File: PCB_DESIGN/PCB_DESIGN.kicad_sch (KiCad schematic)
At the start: 1 part, among them U1 A4988SETTR-T

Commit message: Actualizacion
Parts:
- removed U1: A4988SETTR-T, A4988_motorCtrl:QFN50P500X500X90-29N, symbol A4988SETTR-T:A4988SETTR-T
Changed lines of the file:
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@@
 	(generator_version "8.0")
 	(paper "A4")
-	(symbol
-		(lib_id "A4988SETTR-T:A4988SETTR-T")
-		(at 80.01 78.74 0)
-		(unit 1)
-		(exclude_from_sim no)
-		(in_bom yes)
-		(on_board yes)
-		(dnp no)
-		(fields_autoplaced yes)
-		(property "Reference" "U1"
-			(at 80.01 45.72 0)
-			(effects
-				(font
-					(size 1.27 1.27)
-				)
-			)
-		)
-		(property "Value" "A4988SETTR-T"
-			(at 80.01 48.26 0)
-			(effects
-				(font
-					(size 1.27 1.27)
-				)
-			)
-		)
-		(property "Footprint" "A4988_motorCtrl:QFN50P500X500X90-29N"
-			(at 80.01 78.74 0)
-			(effects
-				(font
-					(size 1.27 1.27)
-				)
-				(justify bottom)
-				(hide yes)
-			)
-		)
-		(property "Datasheet" ""
-			(at 80.01 78.74 0)
-			(effects
-				(font
-					(size 1.27 1.27)
-				)
-				(hide yes)
-			)
-		)
-		(property "Description" ""
-			(at 80.01 78.74 0)
-			(effects
-				(font
-					(size 1.27 1.27)
-				)
-				(hide yes)
-			)
-		)
-		(property "MANUFACTURER" "Allegro MicroSystems"
-			(at 80.01 78.74 0)
-			(effects
-				(font
-					(size 1.27 1.27)
-				)
-				(justify bottom)
-				(hide yes)
-			)
-		)
-		(pin "21"
-		)
-		(pin "8"
-		)
-		(pin "1"
-		)
-		(pin "24"
-		)
-		(pin "23"
-		)
-		(pin "5"
-		)
-		(pin "22"
-		)
-		(pin "29"
-		)
-		(pin "19"
-		)
-		(pin "18"
-		)
-		(pin "13"
-		)
-		(pin "27"
-		)
-		(pin "15"
-		)
-		(pin "10"
-		)
-		(pin "11"
-		)
-		(pin "9"
-		)
-		(pin "3"
-		)
-		(pin "12"
-		)
-		(pin "2"
-		)
-		(pin "26"
-		)
-		(pin "16"
-		)
-		(pin "4"
-		)
-		(pin "6"
-		)
-		(pin "28"
-		)
-		(pin "14"
-		)
-		(pin "17"
-		)
-		(instances
-			(project ""
-				(path "/e56d7197-46c3-4c96-a42c-d0ff3339c143"
-					(reference "U1")
-					(unit 1)
-				)
-			)
-		)
-	)
 	(sheet_instances
 		(path "/"

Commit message: Se actualiza el esquematico de la pcb
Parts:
- added C1, C10, C16, C7, C8: 0.1uF, Capacitor_SMD:C_0603_1608Metric_Pad1.08x0.95mm_HandSolder, symbol Device:C
- added C11, C5, C6, C9: C, Capacitor_SMD:C_0603_1608Metric_Pad1.08x0.95mm_HandSolder, symbol Device:C
- added C12, C14: 470μF, Capacitor_SMD:CP_Elec_4x5.3, symbol Device:C_Polarized
- added C13, C15: 0.1μF, Capacitor_SMD:C_0603_1608Metric_Pad1.08x0.95mm_HandSolder, symbol Device:C
- added C2: 0.47uF, Capacitor_SMD:C_0603_1608Metric_Pad1.08x0.95mm_HandSolder, symbol Device:C
- added C3: 10nF, Capacitor_SMD:C_0603_1608Metric_Pad1.08x0.95mm_HandSolder, symbol Device:C
- added C4: 100uF, Capacitor_SMD:CP_Elec_4x5.3, symbol Device:C_Polarized
- added D1: D_Schottky_Small, Diode_SMD:D_SMA, symbol Device:D_Schottky_Small
- added J1, J2: Screw_Terminal_01x04, Connector_PinHeader_2.54mm:PinHeader_1x04_P2.54mm_Vertical, symbol Connector:Screw_Terminal_01x04
- added L1: 47μH, Inductor_SMD:L_Cenker_CKCS5020, symbol Device:L
- added R1, R2: 0.10, Resistor_SMD:R_0603_1608Metric_Pad0.98x0.95mm_HandSolder, symbol Device:R
- added R3: 10k, Resistor_SMD:R_0603_1608Metric_Pad0.98x0.95mm_HandSolder, symbol Device:R
- added R4, R7, R8, R9: R, Resistor_SMD:R_0603_1608Metric_Pad0.98x0.95mm_HandSolder, symbol Device:R
- added RV1: 10k, Potentiometer_SMD:Potentiometer_Bourns_3314J_Vertical, symbol Device:R_Potentiometer
- added RV2: R_Potentiometer, Connector_PinHeader_2.54mm:PinHeader_1x03_P2.54mm_Vertical, symbol Device:R_Potentiometer
- added SW1, SW3: SW_Push, Connector_PinHeader_2.54mm:PinHeader_1x02_P2.54mm_Vertical, symbol Switch:SW_Push
- added U1: DRV8825PWP, DRV8825:IC_TPS61196PWPRQ1, symbol DRV8825PWP:DRV8825PWP
- added U2: ATmega328P-MM, Package_DFN_QFN:QFN-28-1EP_4x4mm_P0.45mm_EP2.4x2.4mm, symbol MCU_Microchip_ATmega:ATmega328P-MM
- added U3, U5: 74HC14, symbol 74xx:74HC14
- added U6: LM2596S-5, Package_TO_SOT_SMD:TO-263-5_TabPin3, symbol Regulator_Switching:LM2596S-5
- added Y1: 16 Mhz, Crystal:Crystal_SMD_0603-2Pin_6.0x3.5mm, symbol Device:Crystal
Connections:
- new net: R4.1, R7.1, SW1.1
- new net: C3.1, U1.2 (CP2)
- new net: C3.2, U1.1 (CP1)
- new net: RV1.2, U1.12 (AVREF), U1.13 (BVREF)
- new net: C1.1, U1.3 (VCP)
- new net: R1.1, U1.6 (ISENA)
- new net: R2.1, U1.9 (ISENB)
- new net: C9.2, R7.2, U3.1
- new net: R8.1, R9.1, SW3.1
- new net: C11.2, R9.2, U5.1
- new net: C5.1, U2.5 (XTAL1/PB6), Y1.2
- new net: R3.1, U2.25 (~{RESET}/PC6)
- new net: C6.1, U2.6 (XTAL2/PB7), Y1.1
- new net: D1.1 (K), L1.1, U6.2 (OUT)
- new net 24V: C1.2, C10.1, C12.1, C13.1, C16.1, C4.1, U1.11 (VMB), U1.4 (VMA), U6.1 (VIN)
- new net 3.3V: C2.1, RV1.1, U1.15 (V3P3OUT)
- new net 5V: C14.1, C15.1, C7.2, C8.1, J1.1 (Pin_1), L1.2, R3.2, SW1.2, SW3.2, U2.16 (AVCC), U2.3 (VCC), U6.4 (FB)
- new net A1: J2.4 (Pin_4), U1.5 (AOUT1)
- new net A2: J2.3 (Pin_3), U1.7 (AOUT2)
- new net B1: J2.2 (Pin_2), U1.10 (BOUT1)
- new net B2: J2.1 (Pin_1), U1.8 (BOUT2)
- new net DIR: U1.20 (DIR), U2.11 (PB1)
- new net GND: C10.2, C11.1, C12.2, C13.2, C14.2, C15.2, C16.2, C2.2, C4.2, C5.2, C6.2, C7.1, C8.2, C9.1, D1.2 (A), J1.4 (Pin_4), R1.2, R2.2, R4.2, R8.2, RV1.3, RV2.1, U1.14 (GND), U1.28 (GND__1), U1.29 (EXP), U1.30 (EXP__1), U1.31 (EXP__2), U1.32 (EXP__3), U1.33 (EXP__4), U1.34 (EXP__5), U1.35 (EXP__6), U1.36 (EXP__7), U1.37 (EXP__8), U1.38 (EXP__9), U1.39 (EXP__10), U1.40 (EXP__11), U1.41 (EXP__12), U1.42 (EXP__13), U1.43 (EXP__14), U1.44 (EXP__15), U1.45 (EXP__16), U1.46 (EXP__17), U1.47 (EXP__18), U1.48 (EXP__19), U1.49 (EXP__20), U1.50 (EXP__21), U2.18 (GND), U2.29 (GND), U2.4 (GND), U6.3 (GND), U6.5 (~{ON}/OFF)
- new net M1: U1.24 (MODE0)
- new net M2: U1.25 (MODE1), U2.12 (PB2)
- new net M3: U1.26 (MODE2)
- new net NRESET: U1.16 (~{NRESET})
- new net NSLEEP: U1.17 (NSLEEP), U2.14 (PB4)
- new net POT: RV2.2, U2.22 (PC3)
- new net PULSADOR1: U2.13 (PB3)
- new net PULSADOR2: U2.15 (PB5), U3.2, U5.2
- new net PULSADOR3: U2.27 (PD1)
- new net SCL: J1.2 (Pin_2), U2.24 (PC5)
- new net SDA: J1.3 (Pin_3), U2.23 (PC4)
- new net STEP: U1.22 (STEP), U2.1 (PD3)
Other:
- note added: "Lm2596 volt regulator (fixed output) 24Vcc - 5Vcc"

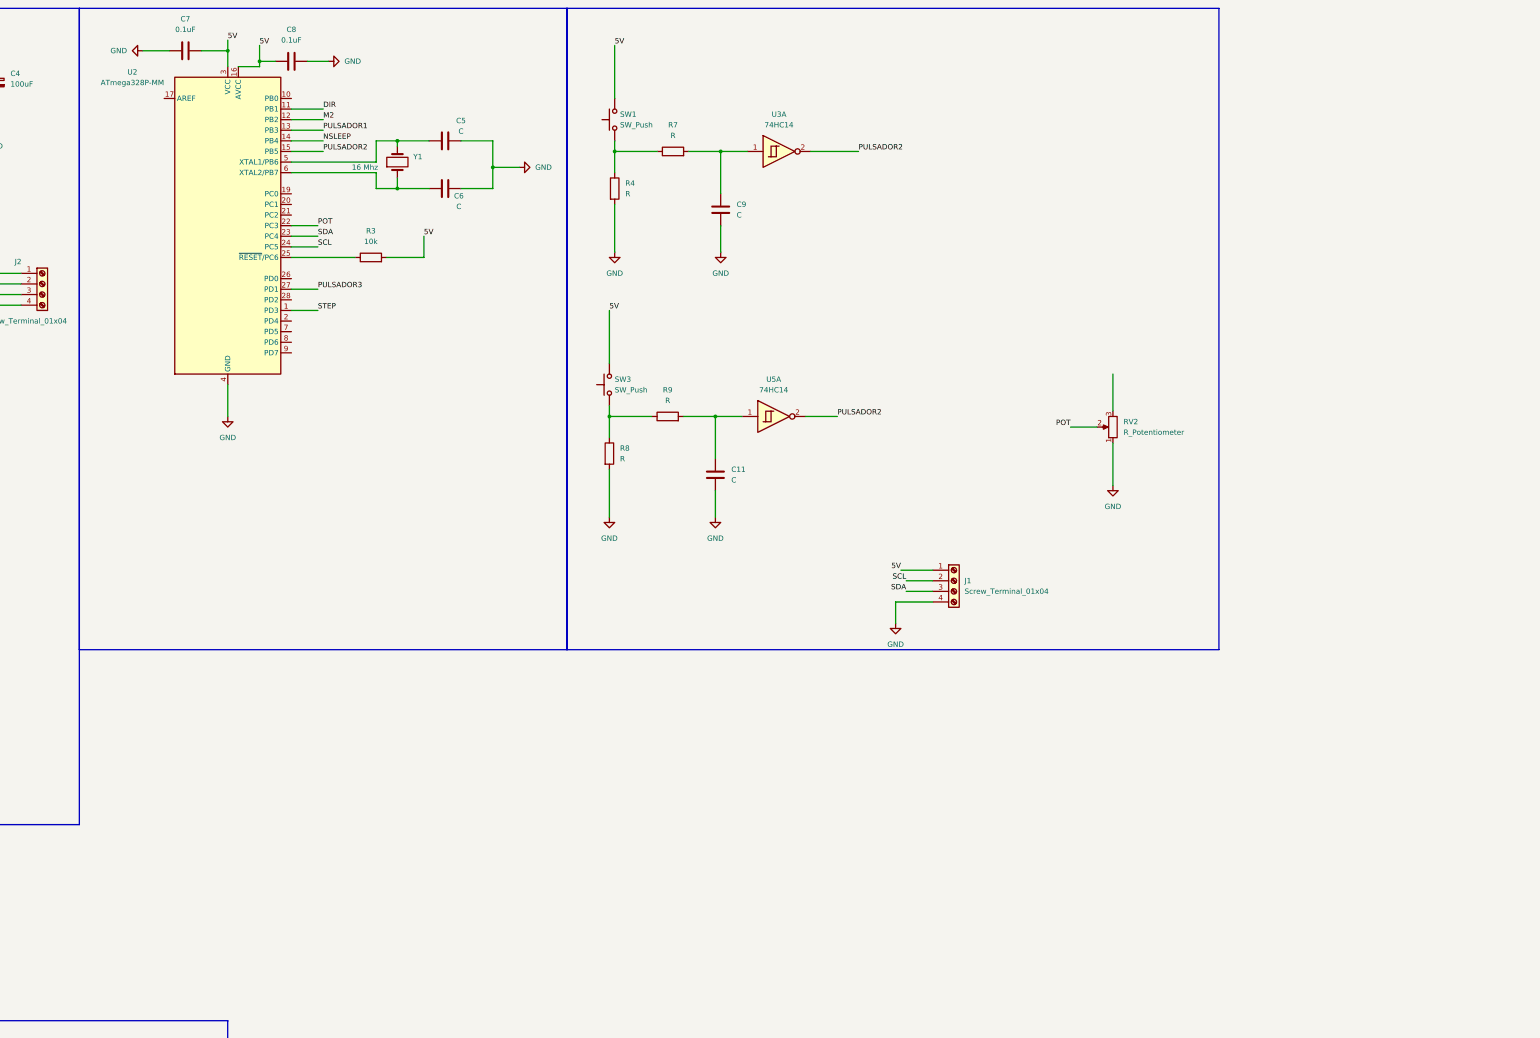
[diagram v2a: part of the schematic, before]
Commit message: Se actualiza el esquematico y se manda a pcb
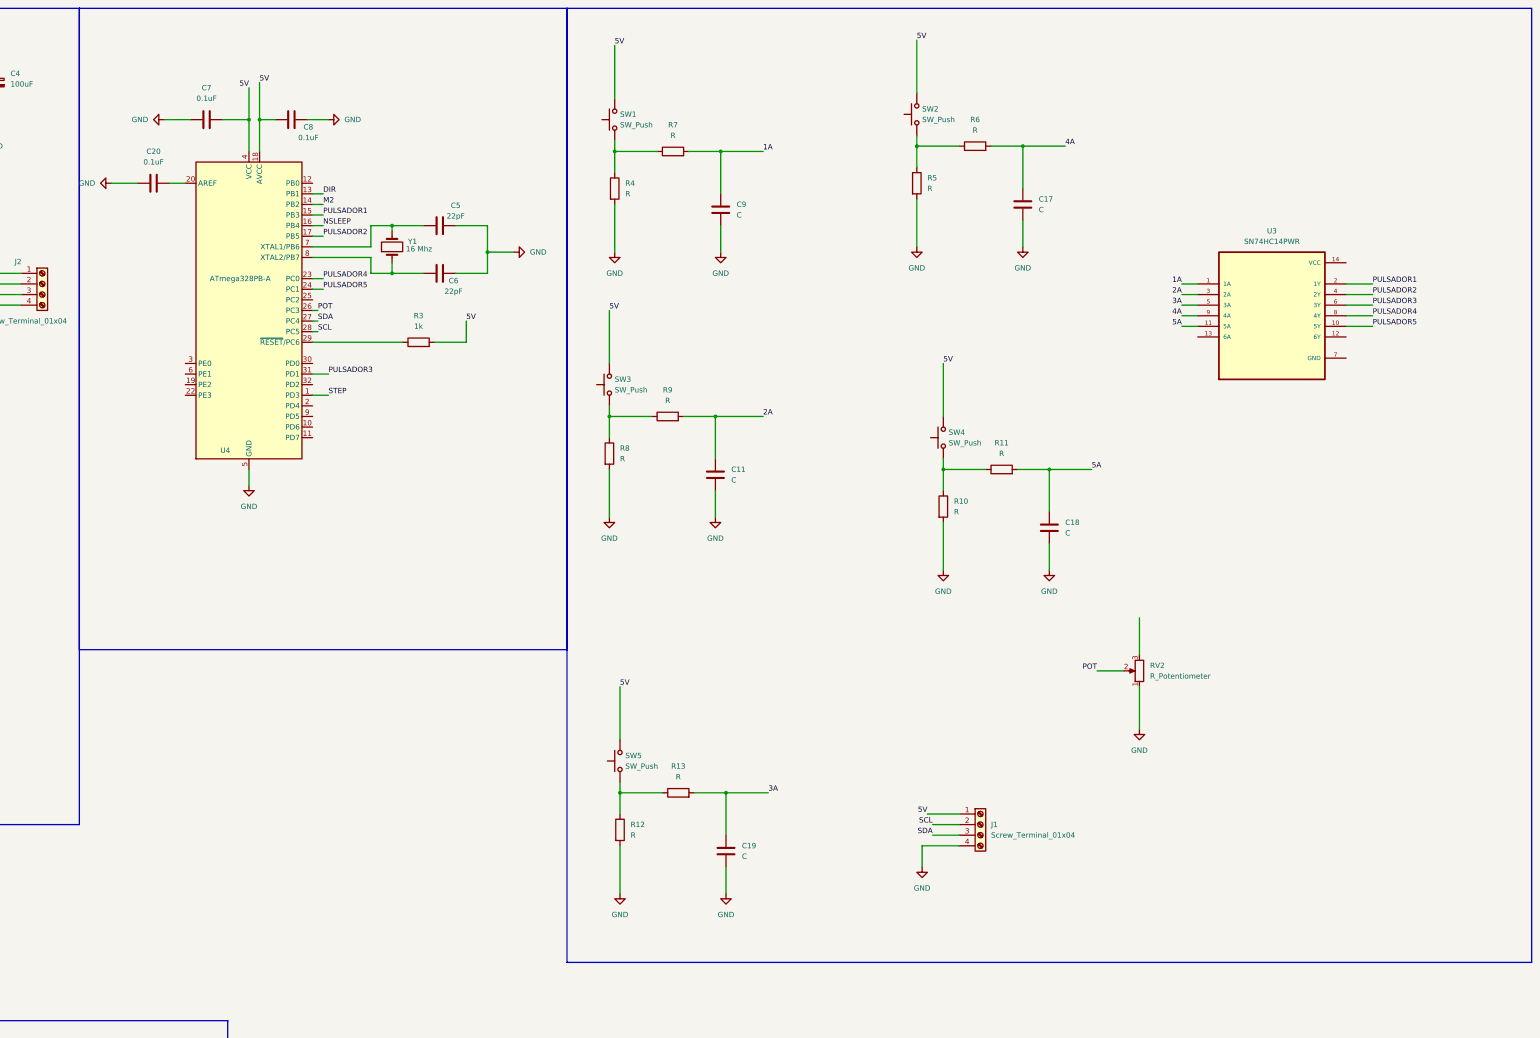
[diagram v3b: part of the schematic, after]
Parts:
- removed U2: ATmega328P-MM, Package_DFN_QFN:QFN-28-1EP_4x4mm_P0.45mm_EP2.4x2.4mm, symbol MCU_Microchip_ATmega:ATmega328P-MM
- removed U3, U5: 74HC14, symbol 74xx:74HC14
- added C17, C18, C19: C, Capacitor_SMD:C_0603_1608Metric_Pad1.08x0.95mm_HandSolder, symbol Device:C
- added C20: 0.1uF, Capacitor_SMD:C_0603_1608Metric_Pad1.08x0.95mm_HandSolder, symbol Device:C
- added R10, R11, R12, R13, R5, R6: R, Resistor_SMD:R_0603_1608Metric_Pad0.98x0.95mm_HandSolder, symbol Device:R
- added SW2, SW4, SW5: SW_Push, Connector_PinHeader_2.54mm:PinHeader_1x02_P2.54mm_Vertical, symbol Switch:SW_Push
- added U3: SN74HC14PWR, SN74HC14PWR:SOP65P640X120-14N, symbol SN74HC14PWR:SN74HC14PWR
- added U4: ATmega328PB-A, Package_QFP:TQFP-32_7x7mm_P0.8mm, symbol MCU_Microchip_ATmega:ATmega328PB-A
- C5, C6: value C -> 22pF
- L1: footprint Inductor_SMD:L_Cenker_CKCS5020 -> INDUCTOR_47uH:IND_SRR1240-470M
- R3: value 10k -> 1k
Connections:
- net 5V: now also SW2.2, SW4.2, SW5.2, U4.18 (AVCC), U4.4 (VCC)
- net DIR: now also U4.13 (PB1)
- net GND: now also C17.1, C18.1, C19.1, C20.1, R10.2, R12.2, R5.2, U4.21 (GND), U4.5 (GND)
- net M2: now also U4.14 (PB2)
- net NSLEEP: now also U4.16 (PB4)
- net POT: now also U4.26 (PC3)
- net PULSADOR1: now also U3.2 (1Y), U4.15 (PB3)
- net PULSADOR2: now also U3.4 (2Y), U4.17 (PB5)
- net PULSADOR3: now also U3.6 (3Y), U4.31 (PD1)
- net SCL: now also U4.28 (PC5)
- net SDA: now also U4.27 (PC4)
- net STEP: now also U4.1 (PD3)
- net 1A: now reaches C9.2, R7.2
- net 1A: now also U3.1 (1A)
- net 2A: now reaches C11.2, R9.2
- net 2A: now also U3.3 (2A)
- net at C5.1, Y1.2: now also U4.7 (XTAL1/PB6)
- net at R3.1: now also U4.29 (~{RESET}/PC6)
- net at C6.1, Y1.1: now also U4.8 (XTAL2/PB7)
- new net: R12.1, R13.1, SW5.1
- new net: R5.1, R6.1, SW2.1
- new net: R10.1, R11.1, SW4.1
- new net: C20.2, U4.20 (AREF)
- new net 3A: C19.2, R13.2, U3.5 (3A)
- new net 4A: C17.2, R6.2, U3.9 (4A)
- new net 5A: C18.2, R11.2, U3.11 (5A)
- new net PULSADOR4: U3.8 (4Y), U4.23 (PC0)
- new net PULSADOR5: U3.10 (5Y), U4.24 (PC1)
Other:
- moved on the sheet: J1, RV2

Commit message: Se agregan pines de programación
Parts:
- added J3: Barrel_Jack_Switch, symbol Connector:Barrel_Jack_Switch
- added J4: Screw_Terminal_01x06, symbol Connector:Screw_Terminal_01x06
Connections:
- net 24V: now also J3.1
- net 5V: now also J4.2 (Pin_2)
- net GND: now also J3.2, J3.3, J4.6 (Pin_6)
- net NSLEEP: now also U4.2 (PD4); no longer U4.16 (PB4)
- net PULSADOR1: now also U4.10 (PD6); no longer U4.15 (PB3)
- net PULSADOR2: now also U4.9 (PD5); no longer U4.17 (PB5)
- net RST: now reaches R3.1, U4.29 (~{RESET}/PC6)
- net RST: now also J4.5 (Pin_5)
- new net MISO: J4.1 (Pin_1), U4.16 (PB4)
- new net MOSI: J4.4 (Pin_4), U4.15 (PB3)
- new net SCK: J4.3 (Pin_3), U4.17 (PB5)

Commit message: Actualizacion de huellas
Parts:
- J3: footprint (none) -> TERMINAL_DC:GCT_DCJ200-10-A-XX-K_REVA
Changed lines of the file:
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@@
 			)
 		)
-		(property "Footprint" ""
+		(property "Footprint" "TERMINAL_DC:GCT_DCJ200-10-A-XX-K_REVA"
 			(at 63.5 291.846 0)
 			(effects
